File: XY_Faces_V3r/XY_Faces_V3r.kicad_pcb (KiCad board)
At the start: 4 copper layers, 83 x 98 mm, 38 parts, among them CN1 DF11-2DSA-4DP, J11 DF11-4DP-2DSA, J13 DF11-4DP-2DSA, J2 Conn_01x01, J3 Conn_01x01, J4 Conn_01x01, J5 Conn_01x01, Q2 CSD17576Q5B, U1 VEML7700, U2 TMP112xxDRL, U3 DRV2605LDGS, U4 TCA4311ADGKR, U5 5040500691, U6 5040500691

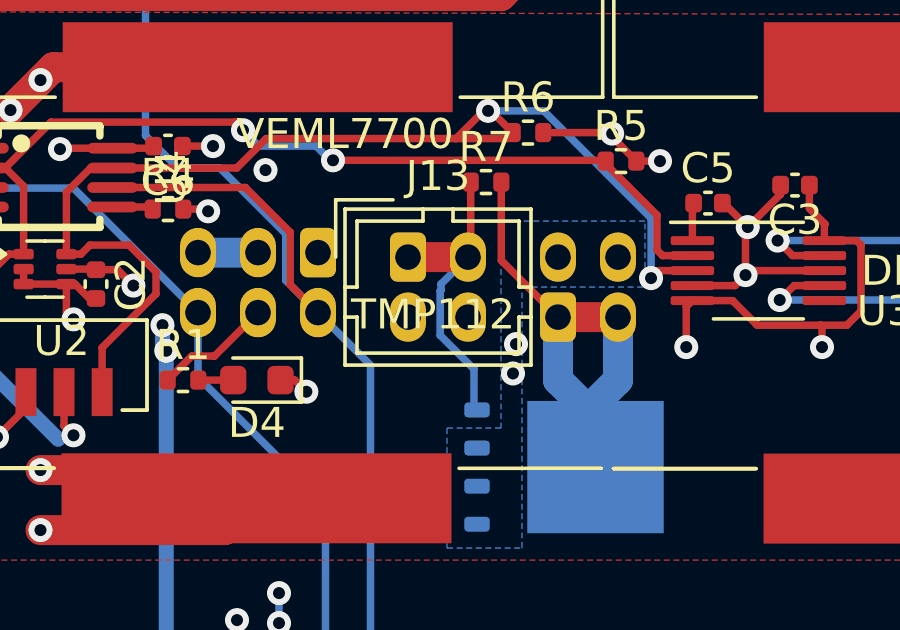
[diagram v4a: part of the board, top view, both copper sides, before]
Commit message: V3r: Updated CAD Model
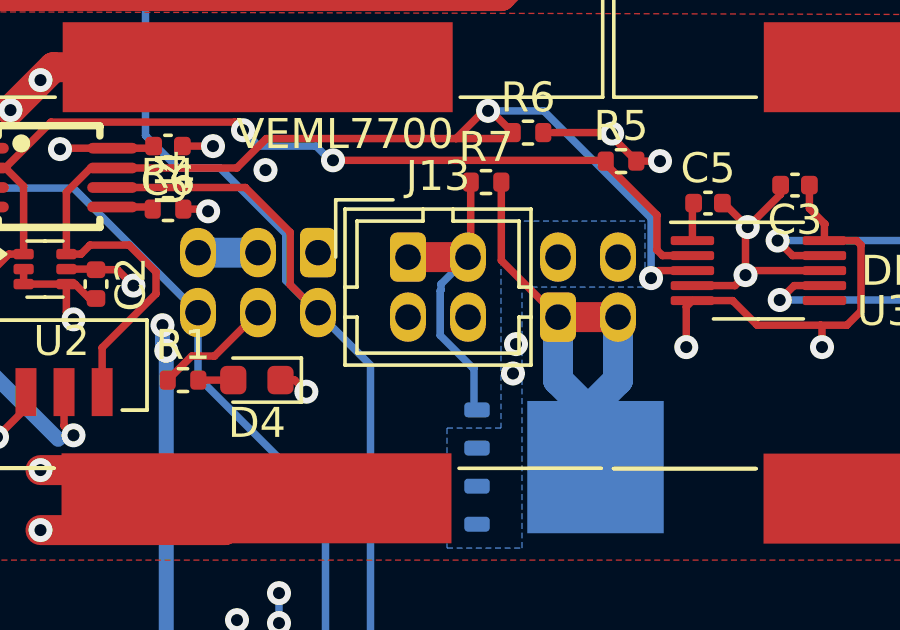
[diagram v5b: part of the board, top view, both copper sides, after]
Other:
- board text removed: "TMP112"
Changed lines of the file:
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@@
 		)
 		(embedded_fonts no)
-		(model "${KIPRJMOD}/Extras/3-DComponents/KXOB201K04F-TR.STEP"
+		(model "../3D Models/Solar Cell.step"
 			(offset
 				(xyz 0 0 0)
@@
 			)
 			(rotate
-				(xyz -90 0 0)
-			)
-		)
-		(model "C:/Users/bronc/Downloads/solar_cell.step"
-			(offset
-				(xyz -3.4 -0.6 0)
-			)
-			(scale
-				(xyz 1 1 1)
-			)
-			(rotate
-				(xyz 0 0 0)
+				(xyz -0 -0 -90)
 			)
 		)
@@
 		)
 		(embedded_fonts no)
-		(model "${KIPRJMOD}/Extras/3-DComponents/KXOB201K04F-TR.STEP"
+		(model "../3D Models/Solar Cell.step"
 			(offset
 				(xyz 0 0 0)
@@
 			)
 			(rotate
-				(xyz -90 0 0)
-			)
-		)
-		(model "C:/Users/bronc/Downloads/solar_cell.step"
-			(offset
-				(xyz -3.3 -0.6 0)
-			)
-			(scale
-				(xyz 1 1 1)
-			)
-			(rotate
-				(xyz 0 0 0)
+				(xyz -0 -0 -90)
 			)
 		)
@@
 			)
 		)
+		(model "/Users/ncc-michael/Documents/KiCad/easyeda2kicad/easyeda2kicad.3dshapes/CONN-TH_DF11-4DP-2DSA-08.step"
+			(offset
+				(xyz 1 -1 0)
+			)
+			(scale
+				(xyz 1 1 1)
+			)
+			(rotate
+				(xyz -0 -0 180)
+			)
+		)
 	)
 	(footprint "SolarPanelBoards:KXOB101K08F-TR"
@@
 		)
 		(embedded_fonts no)
-		(model "${KIPRJMOD}/Extras/3-DComponents/KXOB201K04F-TR.STEP"
+		(model "../3D Models/Solar Cell.step"
 			(offset
 				(xyz 0 0 0)
@@
 			)
 			(rotate
-				(xyz -90 0 0)
-			)
-		)
-		(model "C:/Users/bronc/Downloads/solar_cell.step"
-			(offset
-				(xyz -3.3 -0.6 0)
-			)
-			(scale
-				(xyz 1 1 1)
-			)
-			(rotate
-				(xyz 0 0 0)
+				(xyz -0 -0 -90)
 			)
 		)
@@
 		)
 		(embedded_fonts no)
-		(model "${KIPRJMOD}/Extras/3-DComponents/KXOB201K04F-TR.STEP"
+		(model "../3D Models/Solar Cell.step"
 			(offset
 				(xyz 0 0 0)
@@
 			)
 			(rotate
-				(xyz -90 0 0)
-			)
-		)
-		(model "C:/Users/bronc/Downloads/solar_cell.step"
-			(offset
-				(xyz -3.3 -0.6 0)
-			)
-			(scale
-				(xyz 1 1 1)
-			)
-			(rotate
-				(xyz 0 0 0)
+				(xyz -0 -0 -90)
 			)
 		)
@@
 		)
 		(embedded_fonts no)
-		(model "${KIPRJMOD}/Extras/3-DComponents/KXOB201K04F-TR.STEP"
+		(model "../3D Models/Solar Cell.step"
 			(offset
 				(xyz 0 0 0)
@@
 			)
 			(rotate
-				(xyz -90 0 0)
-			)
-		)
-		(model "C:/Users/bronc/Downloads/solar_cell.step"
-			(offset
-				(xyz -3.3 -0.6 0)
-			)
-			(scale
-				(xyz 1 1 1)
-			)
-			(rotate
-				(xyz 0 0 0)
+				(xyz -0 -0 -90)
 			)
 		)
@@
 		)
 		(embedded_fonts no)
-		(model "${KIPRJMOD}/Extras/3-DComponents/KXOB201K04F-TR.STEP"
+		(model "../3D Models/Solar Cell.step"
 			(offset
 				(xyz 0 0 0)
@@
 			)
 			(rotate
-				(xyz -90 0 0)
-			)
-		)
-		(model "C:/Users/bronc/Downloads/solar_cell.step"
-			(offset
-				(xyz -3.3 -0.6 0)
-			)
-			(scale
-				(xyz 1 1 1)
-			)
-			(rotate
-				(xyz 0 0 0)
+				(xyz -0 -0 -90)
 			)
 		)
@@
 		)
 		(fp_line
-			(start 0.5 1.200001)
+			(start 0.5 1.2)
 			(end 0.5 1.6)
 			(stroke
@@
 		)
 		(fp_line
-			(start -1.7 1.200001)
-			(end 0.5 1.200001)
+			(start -1.7 1.2)
+			(end 0.5 1.2)
 			(stroke
 				(width 0.12)
@@
 		(fp_line
 			(start -1.7 -1)
-			(end -1.7 1.200001)
+			(end -1.7 1.2)
 			(stroke
 				(width 0.12)
@@
 		(fp_line
 			(start -2.41 1.91)
-			(end -0.499999 1.91)
+			(end -0.5 1.91)
 			(stroke
 				(width 0.12)
@@
 		)
 		(fp_line
-			(start 6.500001 2)
-			(end -2.5 2.000001)
+			(start 6.5 2)
+			(end -2.5 2)
 			(stroke
 				(width 0.05)
@@
 		(fp_line
 			(start 6.5 -4)
-			(end 6.500001 2)
+			(end 6.5 2)
 			(stroke
 				(width 0.05)
@@
 		)
 		(fp_line
-			(start -2.5 2.000001)
+			(start -2.5 2)
 			(end -2.5 -4)
 			(stroke
@@
 		)
 		(pad "2" thru_hole oval
-			(at 0 -2.000001 180)
+			(at 0 -2 180)
 			(size 1.2 1.65)
 			(drill 0.85)
@@
 		)
 		(pad "3" thru_hole oval
-			(at 2.000001 0 180)
+			(at 2 0 180)
 			(size 1.2 1.65)
 			(drill 0.85)
@@
 		)
 		(pad "6" thru_hole oval
-			(at 4.000001 -2 180)
+			(at 4 -2 180)
 			(size 1.2 1.65)
 			(drill 0.85)
@@
 		)
 		(embedded_fonts no)
-		(model "${KICAD9_3DMODEL_DIR}/Connector_Hirose.3dshapes/Hirose_DF11-6DP-2DSA_2x03_P2.00mm_Vertical.wrl"
+		(model "/Users/ncc-michael/Documents/KiCad/easyeda2kicad/easyeda2kicad.3dshapes/CONN-TH_DF11-6DP-2DSA-01.step"
 			(offset
-				(xyz 0 0 0)
+				(xyz 2 -1 0)
 			)
 			(scale
@@
 			)
 			(rotate
-				(xyz 0 0 0)
+				(xyz -0 -0 180)
 			)
 		)
@@
 			)
 		)
+		(model "/Users/ncc-michael/Documents/KiCad/easyeda2kicad/easyeda2kicad.3dshapes/CONN-TH_DF11-4DP-2DSA-08.step"
+			(offset
+				(xyz 1 -1 0)
+			)
+			(scale
+				(xyz 1 1 1)
+			)
+			(rotate
+				(xyz -0 -0 180)
+			)
+		)
 	)
 	(footprint "LOGO"
@@
 		)
 	)
-	(gr_text "TMP112"
-		(at 147.6 116.4 0)
-		(layer "F.SilkS")
-		(effects
-			(font
-				(size 1 1)
-				(thickness 0.15)
-			)
-			(justify left bottom)
-		)
-	)

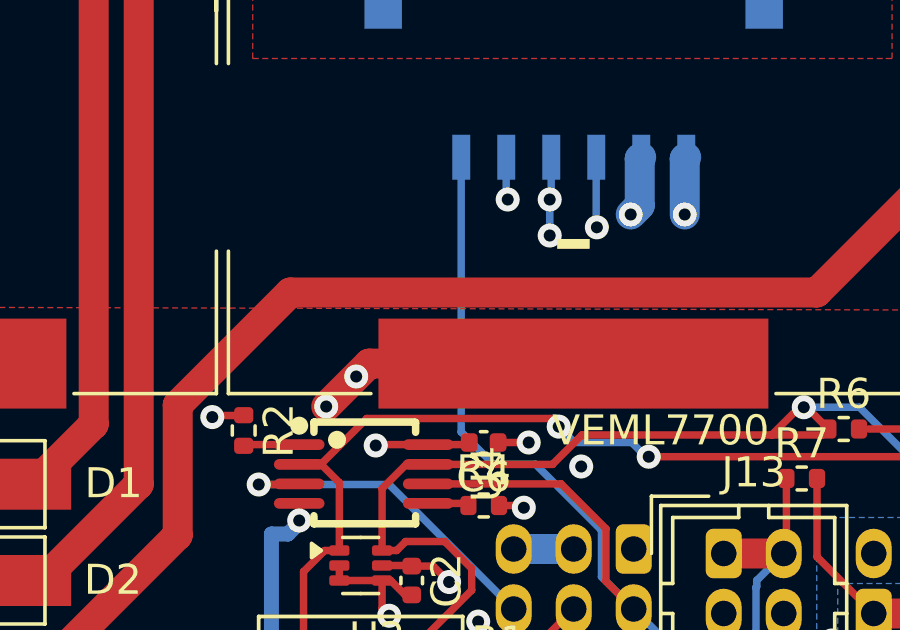
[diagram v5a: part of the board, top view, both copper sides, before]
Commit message: XY V3: Updated Solder Mask
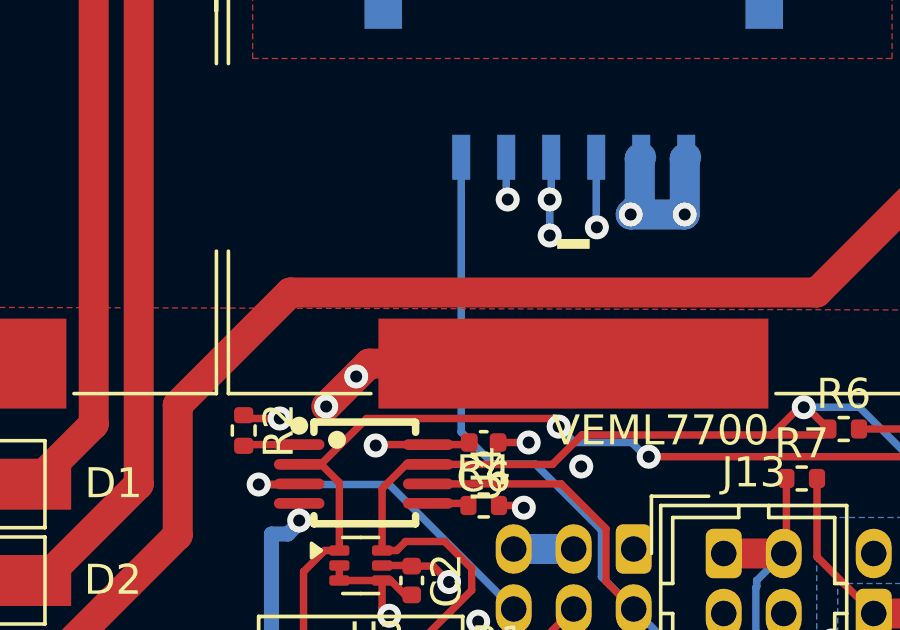
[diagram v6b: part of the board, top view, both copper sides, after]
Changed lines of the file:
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@@
 			(psa4output no)
 			(plot_black_and_white yes)
-			(plotinvisibletext no)
 			(sketchpadsonfab no)
 			(plotpadnumbers no)
@@
 	)
 	(segment
+		(start 133.490001 109.4)
+		(end 133.390001 109.3)
+		(width 0.25)
+		(layer "F.Cu")
+		(net 2)
+	)
+	(segment
 		(start 142.291 117.199)
 		(end 141.49 118)
@@
 	)
 	(segment
-		(start 132.505636 109.3)
-		(end 132.452818 109.352818)
-		(width 0.25)
-		(layer "F.Cu")
-		(net 2)
-	)
-	(segment
 		(start 163.3 116.22)
 		(end 163.25 116.17)
@@
 	)
 	(segment
-		(start 133.390001 109.3)
-		(end 132.505636 109.3)
-		(width 0.25)
-		(layer "F.Cu")
-		(net 2)
-	)
-	(segment
 		(start 158.98 115.35)
 		(end 158.4 115.35)
@@
 	)
 	(segment
+		(start 134.7 109.4)
+		(end 133.490001 109.4)
+		(width 0.25)
+		(layer "F.Cu")
+		(net 2)
+	)
+	(segment
 		(start 163.4 112.8)
 		(end 163.38 112.82)
@@
 	)
 	(via
-		(at 132.452818 109.352818)
+		(at 134.7 109.4)
 		(size 0.8)
 		(drill 0.4)
@@
 	)
 	(segment
+		(start 146.4 102.6)
+		(end 148.2 102.6)
+		(width 1)
+		(layer "B.Cu")
+		(net 3)
+	)
+	(segment
 		(start 141.315878 116.895878)
 		(end 141.442347 117.022347)
@@
 		(width 1)
 		(layer "In1.Cu")
-		(net 3)
-	)
-	(segment
-		(start 146.4 102.6)
-		(end 148.2 102.6)
-		(width 1)
-		(layer "In1.Cu")
